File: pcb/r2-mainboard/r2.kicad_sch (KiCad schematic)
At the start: 0 parts

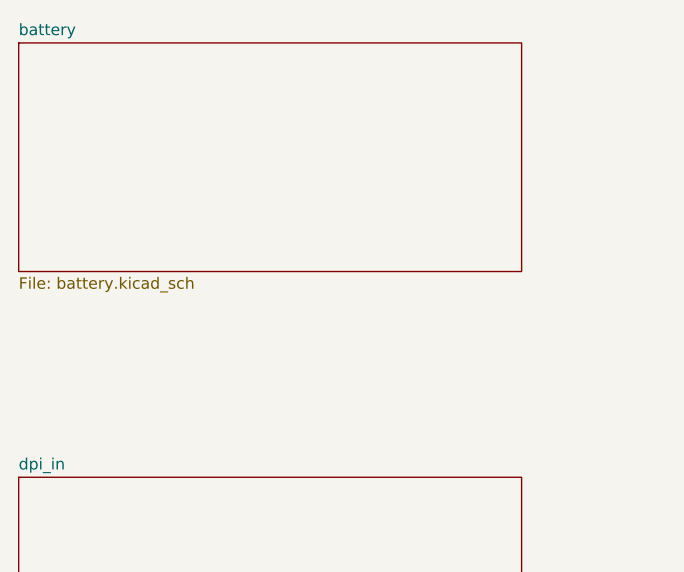
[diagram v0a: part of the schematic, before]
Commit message: R2: capture battery.kicad_sch -- charger, power path, gauge, USB-C
First real sheet of the R2 schematic. ERC reports 16 violations, all of them
'the rest of the board does not exist yet' (12 unconnected sheet pins on the
parent, 4 on CHG_QON# which the MCU and power button drive). No electrical or
structural errors. Netlist exported and read back node by node.

tools/schgen.py is a small KiCad schematic writer built on the kicad-happy
sexp parser: it loads symbol geometry from .kicad_sym, computes absolute pin
coordinates through the placement transform, and emits KiCad 9 format that
'kicad-cli sch upgrade' normalises to KiCad 10. Used once per sheet -- after
a sheet is opened in Eeschema the .kicad_sch is the source of truth.

r2.kicad_sym holds the three symbols KiCad's libraries do not: BQ25892RTW
(derived from the stock BQ25895RTW by renaming pins 2, 3 and 24), MAX17048,
and a flattened USBLC6-2SC6 -- flattened because embedding KiCad's derived
form makes ERC report lib_symbol_mismatch.

Reading the finished netlist found three omissions, now fixed: CE had no
defined level (datasheet requires it be driven, and low enables charging so a
flat cell can recover), OTG could float into boost mode, and the gauge's
open-drain ALRT had no pull-up.

Co-Authored-By: Claude Opus 5 <noreply@anthropic.com>
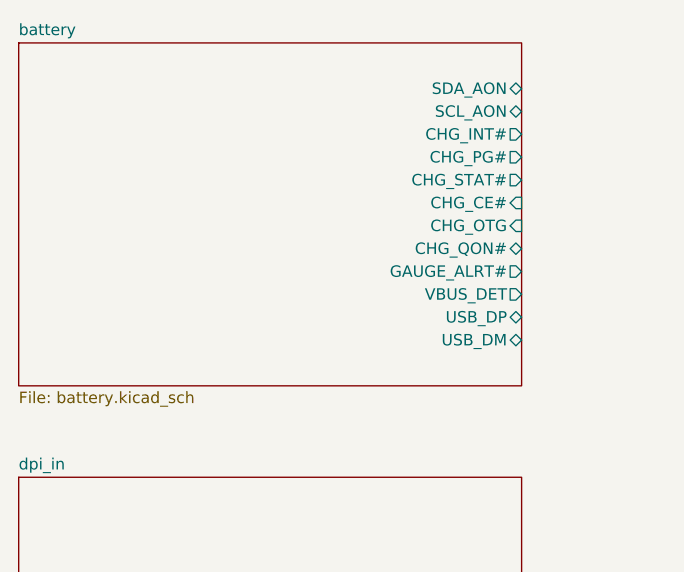
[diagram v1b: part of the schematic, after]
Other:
- sheet battery ports: added CHG_CE#, CHG_INT#, CHG_OTG, CHG_PG#, CHG_QON#, CHG_STAT#, GAUGE_ALRT#, SCL_AON, SDA_AON, USB_DM, USB_DP, VBUS_DET; removed none
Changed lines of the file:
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@@
 	(sheet
 		(at 22.86 30.48)
-		(size 55.88 25.4)
+		(size 55.88 38.1)
 		(exclude_from_sim no)
 		(in_bom yes)
@@
 		)
 		(property "Sheetfile" "battery.kicad_sch"
-			(at 22.86 56.4646 0)
+			(at 22.86 69.1646 0)
 			(show_name no)
 			(do_not_autoplace no)
@@
 			)
 		)
+		(pin "SDA_AON" bidirectional
+			(at 78.74 35.56 0)
+			(effects
+				(font
+					(size 1.27 1.27)
+				)
+				(justify right)
+			)
+		)
+		(pin "SCL_AON" bidirectional
+			(at 78.74 38.1 0)
+			(effects
+				(font
+					(size 1.27 1.27)
+				)
+				(justify right)
+			)
+		)
+		(pin "CHG_INT#" output
+			(at 78.74 40.64 0)
+			(effects
+				(font
+					(size 1.27 1.27)
+				)
+				(justify right)
+			)
+		)
+		(pin "CHG_PG#" output
+			(at 78.74 43.18 0)
+			(effects
+				(font
+					(size 1.27 1.27)
+				)
+				(justify right)
+			)
+		)
+		(pin "CHG_STAT#" output
+			(at 78.74 45.72 0)
+			(effects
+				(font
+					(size 1.27 1.27)
+				)
+				(justify right)
+			)
+		)
+		(pin "CHG_CE#" input
+			(at 78.74 48.26 0)
+			(effects
+				(font
+					(size 1.27 1.27)
+				)
+				(justify right)
+			)
+		)
+		(pin "CHG_OTG" input
+			(at 78.74 50.8 0)
+			(effects
+				(font
+					(size 1.27 1.27)
+				)
+				(justify right)
+			)
+		)
+		(pin "CHG_QON#" bidirectional
+			(at 78.74 53.34 0)
+			(effects
+				(font
+					(size 1.27 1.27)
+				)
+				(justify right)
+			)
+		)
+		(pin "GAUGE_ALRT#" output
+			(at 78.74 55.88 0)
+			(effects
+				(font
+					(size 1.27 1.27)
+				)
+				(justify right)
+			)
+		)
+		(pin "VBUS_DET" output
+			(at 78.74 58.42 0)
+			(effects
+				(font
+					(size 1.27 1.27)
+				)
+				(justify right)
+			)
+		)
+		(pin "USB_DP" bidirectional
+			(at 78.74 60.96 0)
+			(effects
+				(font
+					(size 1.27 1.27)
+				)
+				(justify right)
+			)
+		)
+		(pin "USB_DM" bidirectional
+			(at 78.74 63.5 0)
+			(effects
+				(font
+					(size 1.27 1.27)
+				)
+				(justify right)
+			)
+		)

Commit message: R2: capture power.kicad_sch -- the gated rail tree from +VSYS
WP2. Five converters, every one of them switchable, which is the whole
reason R2 exists: R1 wires four bucks' ~SHDN to +5V and 82% of idle
power sits on rails no firmware can reach.

  +3V3_AON   TPS7A0233   LDO, always on, 25 nA
  +5V_DCDC   TPS61022    boost, behind a TPS22965 load switch
  +3V3_DCDC  TPS63802    buck-boost
  +1V2_DCDC  TPS62A02    buck
  +1V35_DCDC TPS62A02    buck

Two findings changed the plan and are recorded in NOTES-R2-plan.md:

- A 1S cell cannot buck to 3.3 V. +VSYS runs 4.4 V down to 3.0 V, so a
  step-down converter drops out halfway down the discharge curve. +3V3
  is a buck-boost, and the two 3.3 V rails the plan called for become
  one, since each would cost a whole converter.
- A boost has no load disconnect. Disabling TPS61022 alone would leave
  ~3.4 V on the SoM's VIN pin, which is a partial-power state rather
  than off, so the disconnect goes on the boost's input instead.

Every EN carries a pull-down; the rails come up only when firmware asks.
PG pull-ups are 470k, not 10k, because a power-good pin is low whenever
its rail is off -- at 10k that is 3.3 mW of the 10 mW standby budget.
Converter overhead in standby works out to ~24 uA.

Verified with kicad-cli erc plus a node-by-node read of the exported
netlist. 25 violations, one of them real: battery.kicad_sch's +3V3_AON
PWR_FLAG is now redundant against U10's power_out pin. Left in place --
that sheet is out for review and editing it under an open Eeschema
session would discard unsaved work. docs/power.md §9 has the one-symbol
fix.

Nothing here has been built or measured.

Co-Authored-By: Claude Opus 5 <noreply@anthropic.com>
Claude-Session: https://claude.ai/code/session_01LsKada4AAxqV6Vzap4hwJf
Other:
- sheet power ports: added MCU_EN_3V3, MCU_EN_5V, MCU_EN_DDR, MCU_EN_FPGA_CORE, PG_1V2, PG_1V35, PG_3V3; removed none
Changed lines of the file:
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@@
+			)
+		)
+		(pin "MCU_EN_5V" input
+			(at 177.8 35.56 0)
+			(effects
+				(font
+					(size 1.27 1.27)
+				)
+				(justify right)
+			)
+		)
+		(pin "MCU_EN_3V3" input
+			(at 177.8 38.1 0)
+			(effects
+				(font
+					(size 1.27 1.27)
+				)
+				(justify right)
+			)
+		)
+		(pin "MCU_EN_FPGA_CORE" input
+			(at 177.8 40.64 0)
+			(effects
+				(font
+					(size 1.27 1.27)
+				)
+				(justify right)
+			)
+		)
+		(pin "MCU_EN_DDR" input
+			(at 177.8 43.18 0)
+			(effects
+				(font
+					(size 1.27 1.27)
+				)
+				(justify right)
+			)
+		)
+		(pin "PG_3V3" output
+			(at 177.8 45.72 0)
+			(effects
+				(font
+					(size 1.27 1.27)
+				)
+				(justify right)
+			)
+		)
+		(pin "PG_1V2" output
+			(at 177.8 48.26 0)
+			(effects
+				(font
+					(size 1.27 1.27)
+				)
+				(justify right)
+			)
+		)
+		(pin "PG_1V35" output
+			(at 177.8 50.8 0)
+			(effects
+				(font
+					(size 1.27 1.27)
+				)
+				(justify right)
 			)
 		)

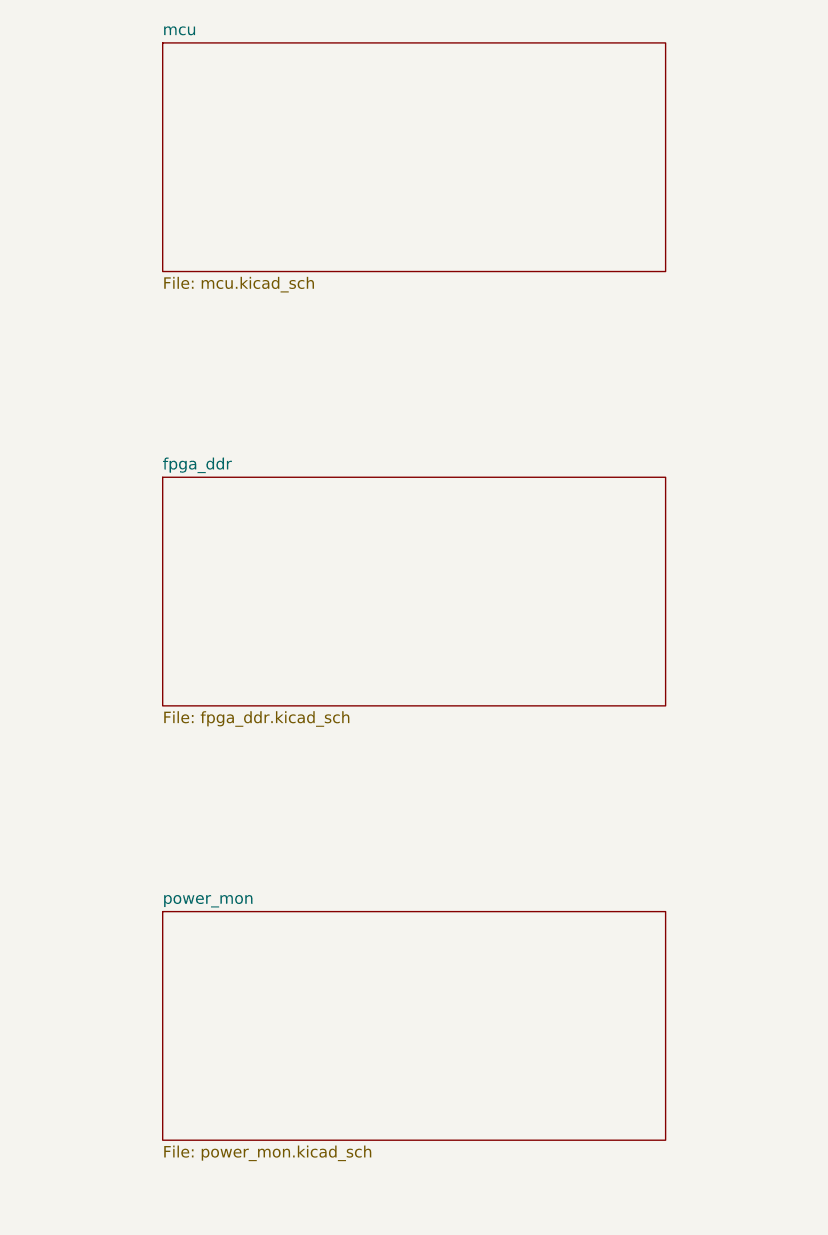
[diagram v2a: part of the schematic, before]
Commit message: R2: capture mcu.kicad_sch -- STM32G0 housekeeping and the pin assignment
WP3. The sheet is small; the deliverable is the pin assignment, which is
one-shot because STM32 peripheral functions are fixed to particular pins.
Every choice is checked against datasheets/stm32g0b1.pdf (DS13560 Rev 1)
Table 12 column "LQFP64 - GP" and Tables 13-20.

STM32G0B1RCT6, LQFP-64, C3034735 (6029 in stock, $1.67). Chosen for its two
12-bit DACs -- R1 drives VCOM and VGH from DAC_CHANNEL_1/2, and most of the
G0 line has no DAC -- and for 60 I/O against a signal count of 49. Stop 1
with the RTC running is 3.7 uA typ, so the always-on domain costs ~14 uW.

Two decisions worth the reading:

- The SoM, not the MCU, drives Caster's CSR bus. Caster/rtl/csr.v is a 4-wire
  SPI slave carrying waveform LUTs, OSD bitmaps and per-page op commands; R1
  held that data in SPIFFS beside the MCU, and R2 deletes that flash. The MCU
  keeps only FPGA_PROG#/DONE/SUSP, which are power-domain signals. Decided by
  the hardware owner.
- The power button never touches the MCU's supply domain. QON idles at 4.3 V
  behind a 200 k internal pull-up (bq25890.pdf), and in ship mode +3V3_AON
  does not exist at all -- so SW20 shorts QON straight to GND, the MCU only
  listens through R41, and PD6 must have its internal pulls disabled.

EXTI lines are deconflicted by hand: on G0 an EXTI line is selected by pin
number across all ports, so the three wake sources and four charger inputs
each take a distinct index. That constraint is invisible in a pin count.

Verified: ERC 186 violations, one real (the +3V3_AON PWR_FLAG on the battery
sheet, still yours to delete); a script re-read the exported netlist and
asserted all 50 assignments land on the port they claim and that the
unconnected set is exactly the 11 reserved pins; cross-sheet names and
directions match power and battery exactly. battery.kicad_sch and
power.kicad_sch are untouched.

Co-Authored-By: Claude Opus 5 <noreply@anthropic.com>
Claude-Session: https://c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
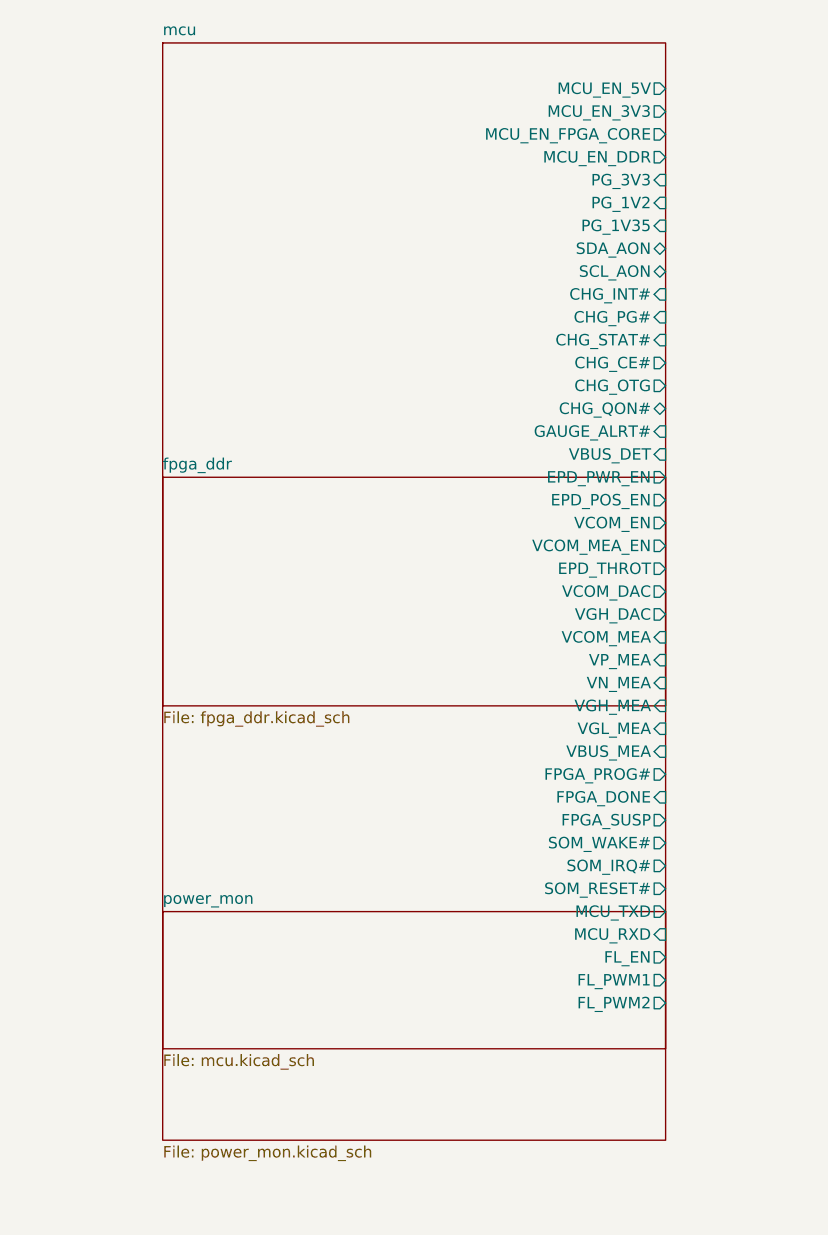
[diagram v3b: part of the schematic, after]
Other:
- sheet mcu ports: added CHG_CE#, CHG_INT#, CHG_OTG, CHG_PG#, CHG_QON#, CHG_STAT#, EPD_POS_EN, EPD_PWR_EN, EPD_THROT, FL_EN, FL_PWM1, FL_PWM2, FPGA_DONE, FPGA_PROG#, FPGA_SUSP, GAUGE_ALRT#, MCU_EN_3V3, MCU_EN_5V, MCU_EN_DDR, MCU_EN_FPGA_CORE, MCU_RXD, MCU_TXD, PG_1V2, PG_1V35, PG_3V3, SCL_AON, SDA_AON, SOM_IRQ#, SOM_RESET#, SOM_WAKE#, VBUS_DET, VBUS_MEA, VCOM_DAC, VCOM_EN, VCOM_MEA, VCOM_MEA_EN, VGH_DAC, VGH_MEA, VGL_MEA, VN_MEA, VP_MEA; removed none
